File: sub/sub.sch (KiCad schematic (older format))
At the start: 17 parts, among them J1 YG_IN, J2 YG_OUT, J3 PBB_IN, J4 PBB_OUT, J5 PRR_IN, J6 PRR_OUT, J7 SYNC_IN, J8 SYNC_OUT, J9 Conn_01x05, SW1 SW_YG_TERM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

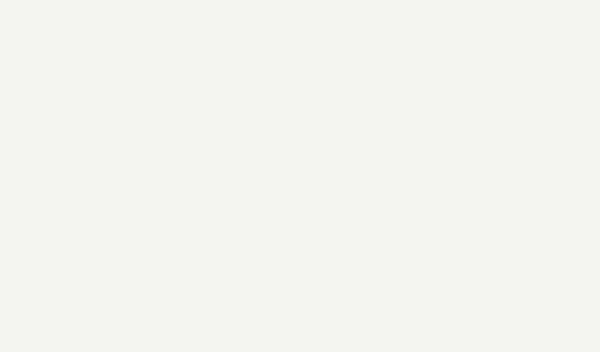
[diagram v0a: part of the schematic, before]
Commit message: Use proper mounting holes rather than edge cuts
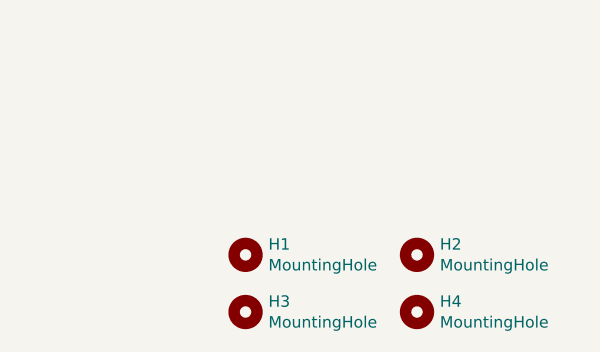
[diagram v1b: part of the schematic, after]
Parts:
- added H1, H2, H3, H4: MountingHole, MountingHole:MountingHole_3.2mm_M3, symbol Mechanical:MountingHole
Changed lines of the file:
@@
+	1    0    0    -1
+$EndComp
+$Comp
+L Mechanical:MountingHole H1
+U 1 1 63472EA2
+P 9750 6100
+F 0 "H1" H 9850 6146 50  0000 L CNN
+F 1 "MountingHole" H 9850 6055 50  0000 L CNN
+F 2 "MountingHole:MountingHole_3.2mm_M3" H 9750 6100 50  0001 C CNN
+F 3 "~" H 9750 6100 50  0001 C CNN
+	1    9750 6100
+	1    0    0    -1
+$EndComp
+$Comp
+L Mechanical:MountingHole H2
+U 1 1 63475570
+P 10500 6100
+F 0 "H2" H 10600 6146 50  0000 L CNN
+F 1 "MountingHole" H 10600 6055 50  0000 L CNN
+F 2 "MountingHole:MountingHole_3.2mm_M3" H 10500 6100 50  0001 C CNN
+F 3 "~" H 10500 6100 50  0001 C CNN
+	1    10500 6100
+	1    0    0    -1
+$EndComp
+$Comp
+L Mechanical:MountingHole H3
+U 1 1 63475802
+P 9750 6350
+F 0 "H3" H 9850 6396 50  0000 L CNN
+F 1 "MountingHole" H 9850 6305 50  0000 L CNN
+F 2 "MountingHole:MountingHole_3.2mm_M3" H 9750 6350 50  0001 C CNN
+F 3 "~" H 9750 6350 50  0001 C CNN
+	1    9750 6350
+	1    0    0    -1
+$EndComp
+$Comp
+L Mechanical:MountingHole H4
+U 1 1 63475BFD
+P 10500 6350
+F 0 "H4" H 10600 6396 50  0000 L CNN
+F 1 "MountingHole" H 10600 6305 50  0000 L CNN
+F 2 "MountingHole:MountingHole_3.2mm_M3" H 10500 6350 50  0001 C CNN
+F 3 "~" H 10500 6350 50  0001 C CNN
+	1    10500 6350
 	1    0    0    -1
 $EndComp
